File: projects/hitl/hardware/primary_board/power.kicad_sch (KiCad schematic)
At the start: 11 parts, among them J20 CONN_01X03, U9 LT3045

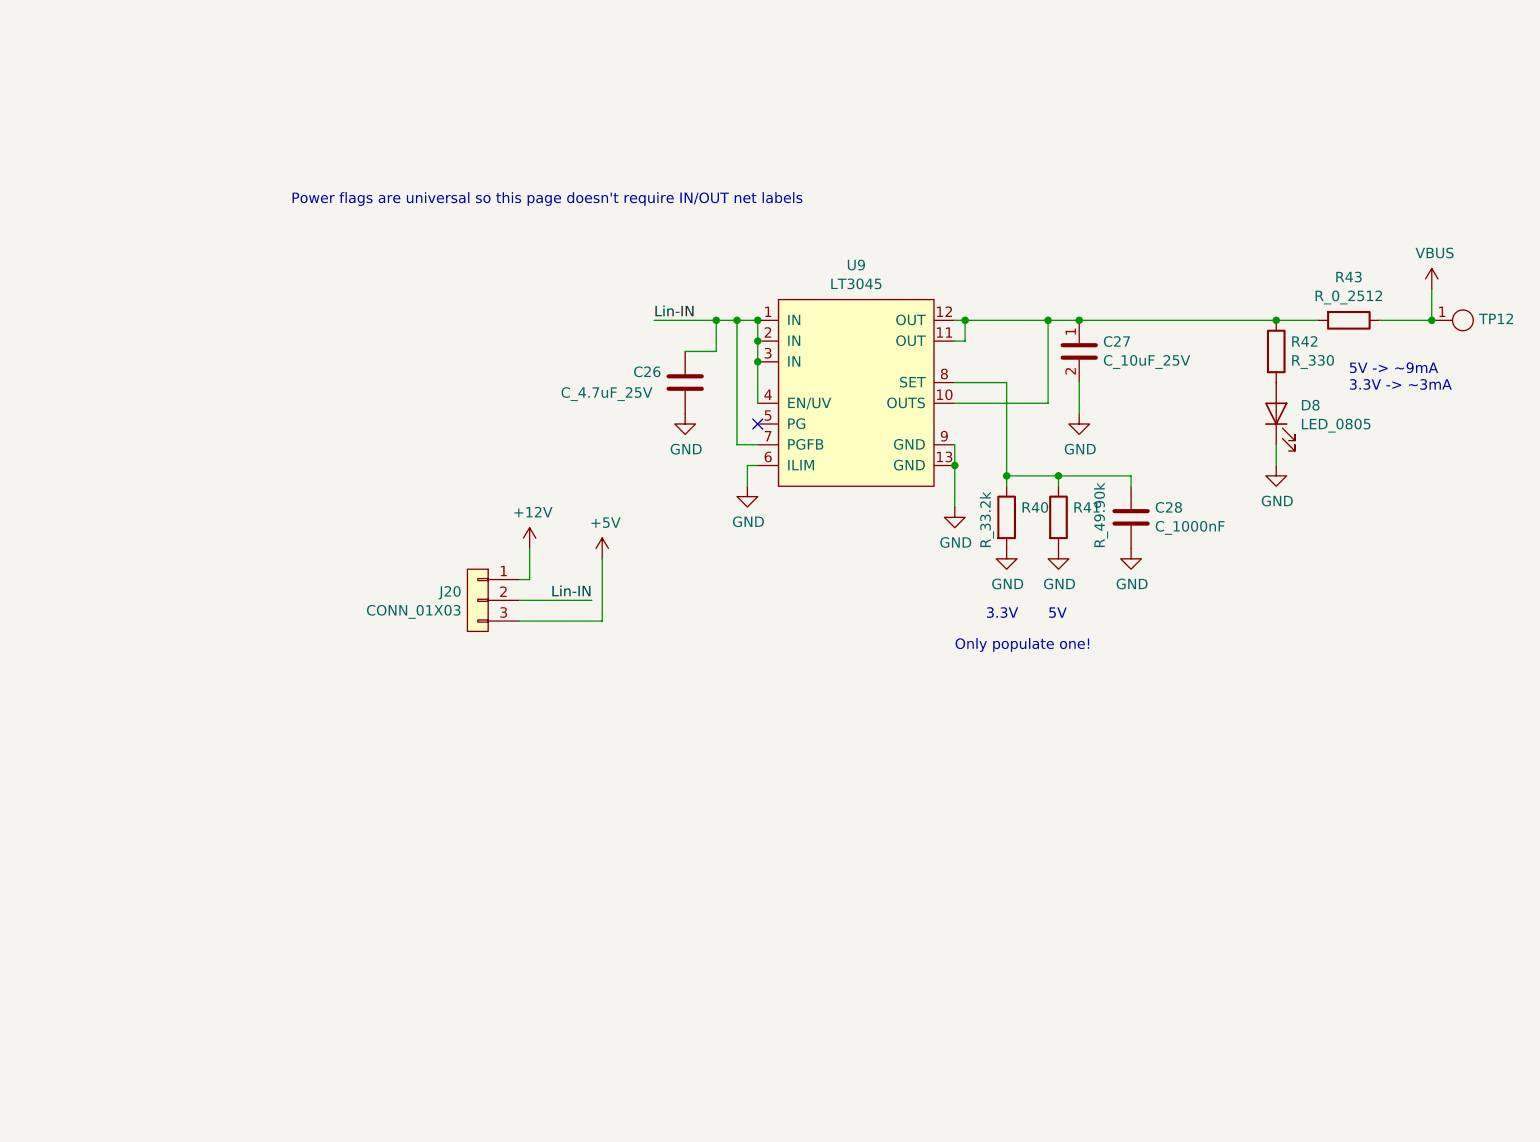
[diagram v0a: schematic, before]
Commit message: Split schematic into sheets
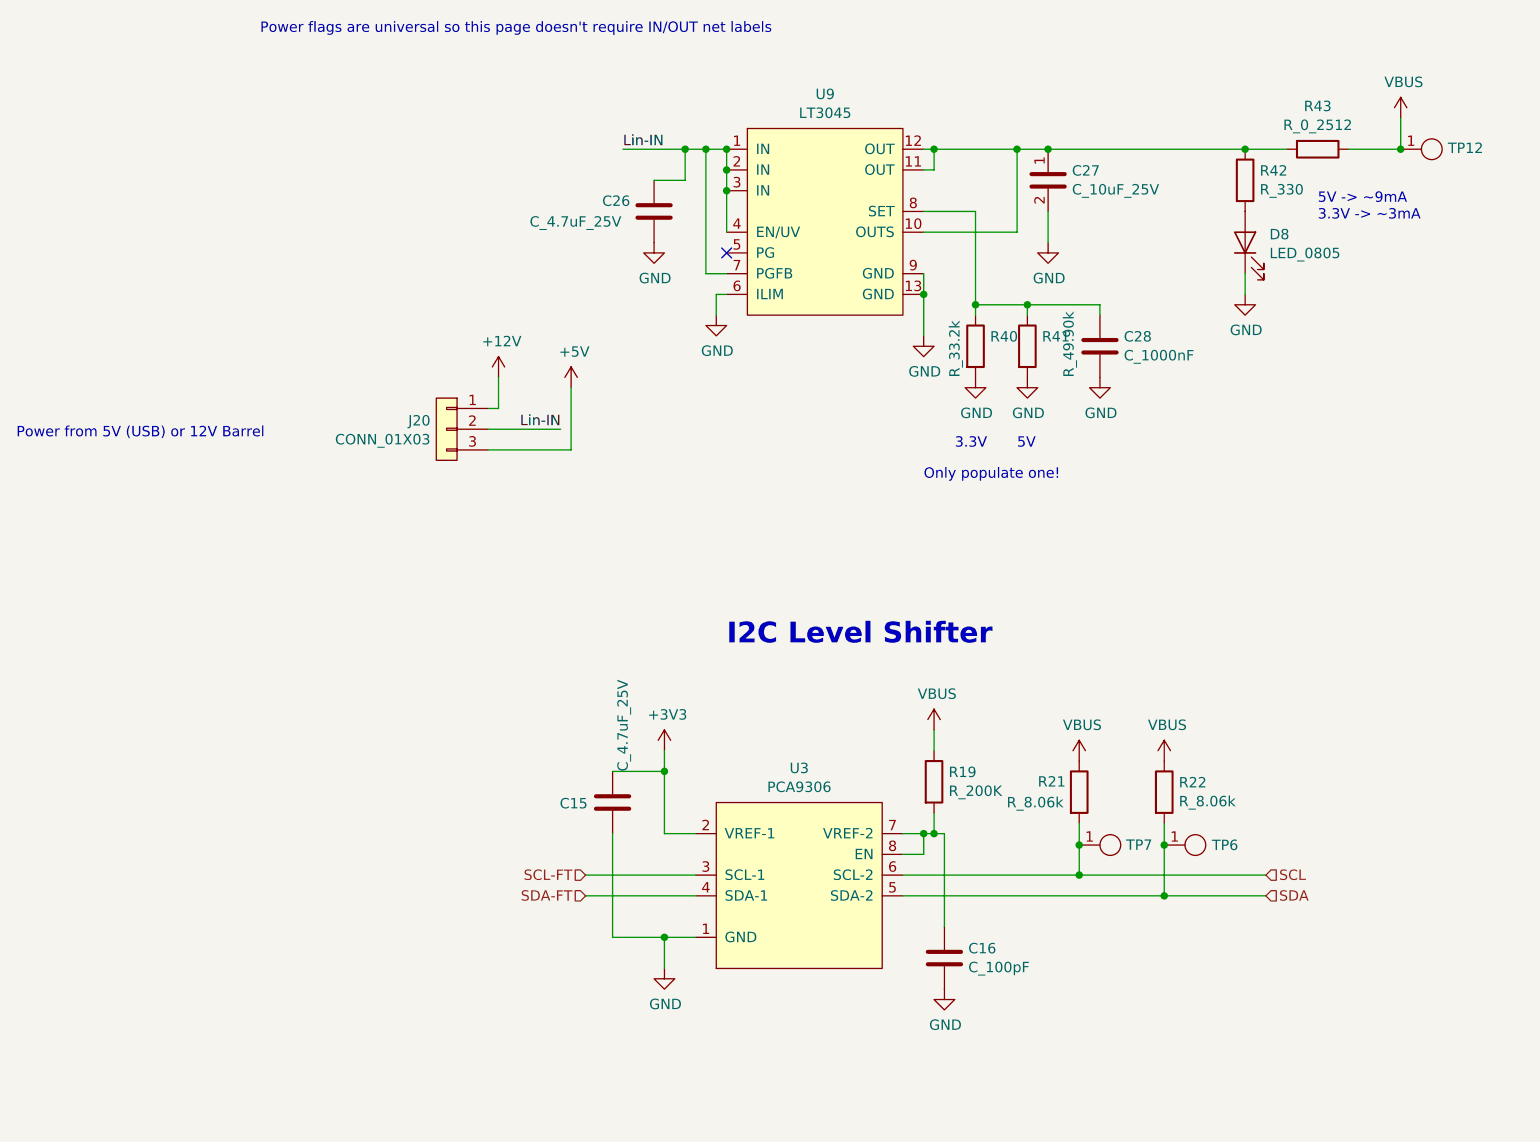
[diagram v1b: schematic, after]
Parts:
- added C15: C_4.7uF_25V, footprints:C_0805_OEM, symbol formula:C_4.7uF_25V
- added C16: C_100pF, footprints:C_0805_OEM, symbol formula:C_100pF
- added R19: R_200K, footprints:R_0805_OEM, symbol formula:R_200K
- added R21, R22: R_8.06k, footprints:R_0805_OEM, symbol formula:R_8.06k
- added TP6, TP7: Test_Point_SMD, footprints:Test_Point_SMD, symbol formula:Test_Point_SMD
- added U3: PCA9306, footprints:SOP50P310X90-8N_pca9306, symbol formula:PCA9306
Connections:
- net GND: now also C15.2, C16.2, U3.1 (GND)
- net VBUS: now also R19.1, R21.1, R22.1
- new net: C16.1, R19.2, U3.7 (VREF-2), U3.8 (EN)
- new net +3V3: C15.1, U3.2 (VREF-1)
- new net SCL: R21.2, TP7.1, U3.6 (SCL-2)
- new net SCL-FT: U3.3 (SCL-1)
- new net SDA: R22.2, TP6.1, U3.5 (SDA-2)
- new net SDA-FT: U3.4 (SDA-1)
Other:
- note added: "I2C Level Shifter"
- note added: "Power from 5V (USB) or 12V Barrel"
- moved on the sheet: C26, C27, C28, D8, J20, R40, R41, R42, R43, TP12, U9

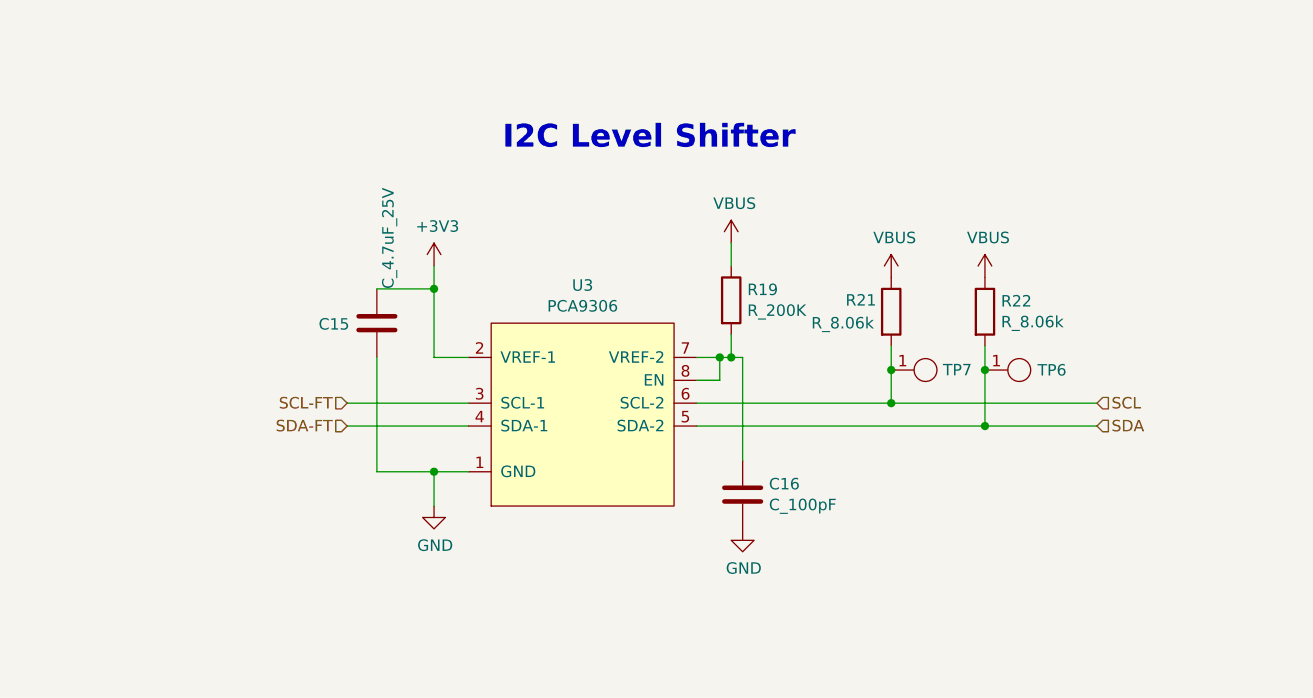
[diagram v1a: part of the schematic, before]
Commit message: Switch FTPROG to button and update I2C level shifter
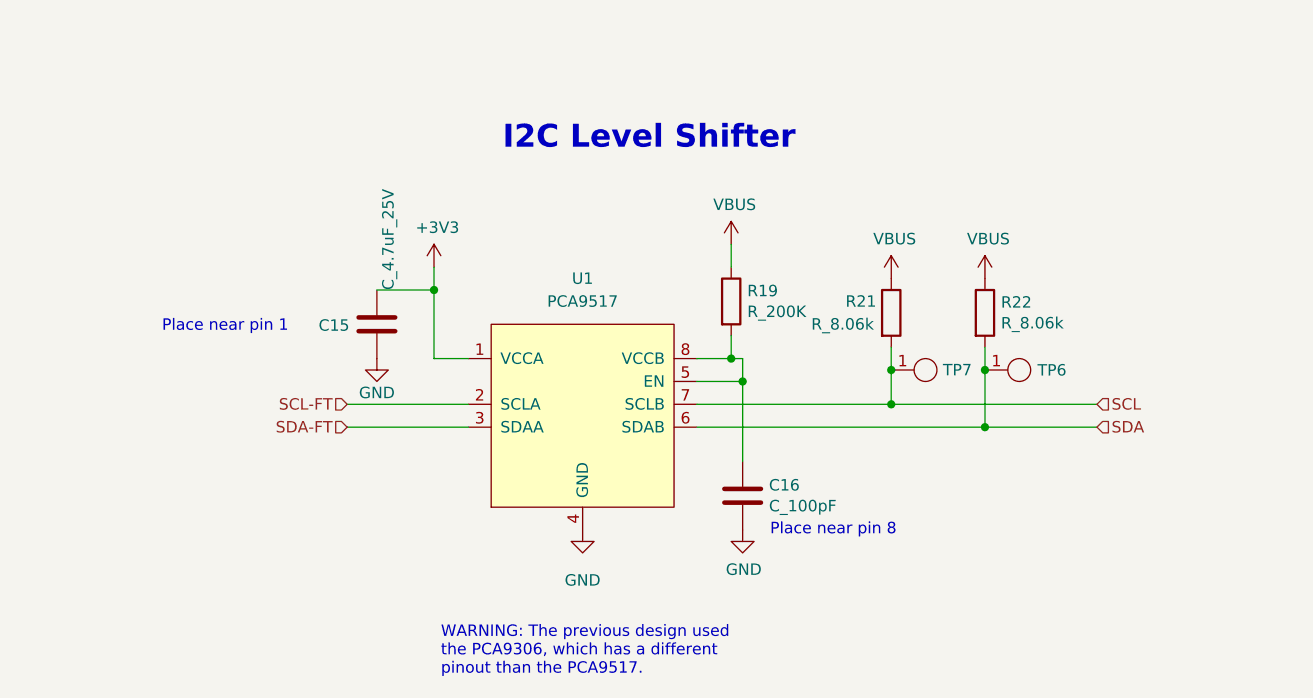
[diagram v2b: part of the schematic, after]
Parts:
- removed U3: PCA9306, footprints:SOP50P310X90-8N_pca9306, symbol formula:PCA9306
- added U1: PCA9517, footprints:Micro8_PCA9517, symbol formula:PCA9517
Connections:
- net +3V3: now also U1.1 (VCCA)
- net GND: now also U1.4 (GND)
- net SCL: now also U1.7 (SCLB)
- net SCL-FT: now also U1.2 (SCLA)
- net SDA: now also U1.6 (SDAB)
- net SDA-FT: now also U1.3 (SDAA)
- net at C16.1, R19.2: now also U1.5 (EN), U1.8 (VCCB)
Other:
- note added: "Place near pin 1"
- note added: "Place near pin 8"
- note added: "WARNING: The previous design used the PCA9306, which has a different pinout than the PCA9517."
